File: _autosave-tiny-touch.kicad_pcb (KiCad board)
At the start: 2 copper layers, 100.3 x 76 mm, 122 parts, among them IC1 STM32F072VBT6, Q1 DTC123J, SW1 SW_Push, U1 MCP1700-3002E_SOT23, U2 SRV05-4

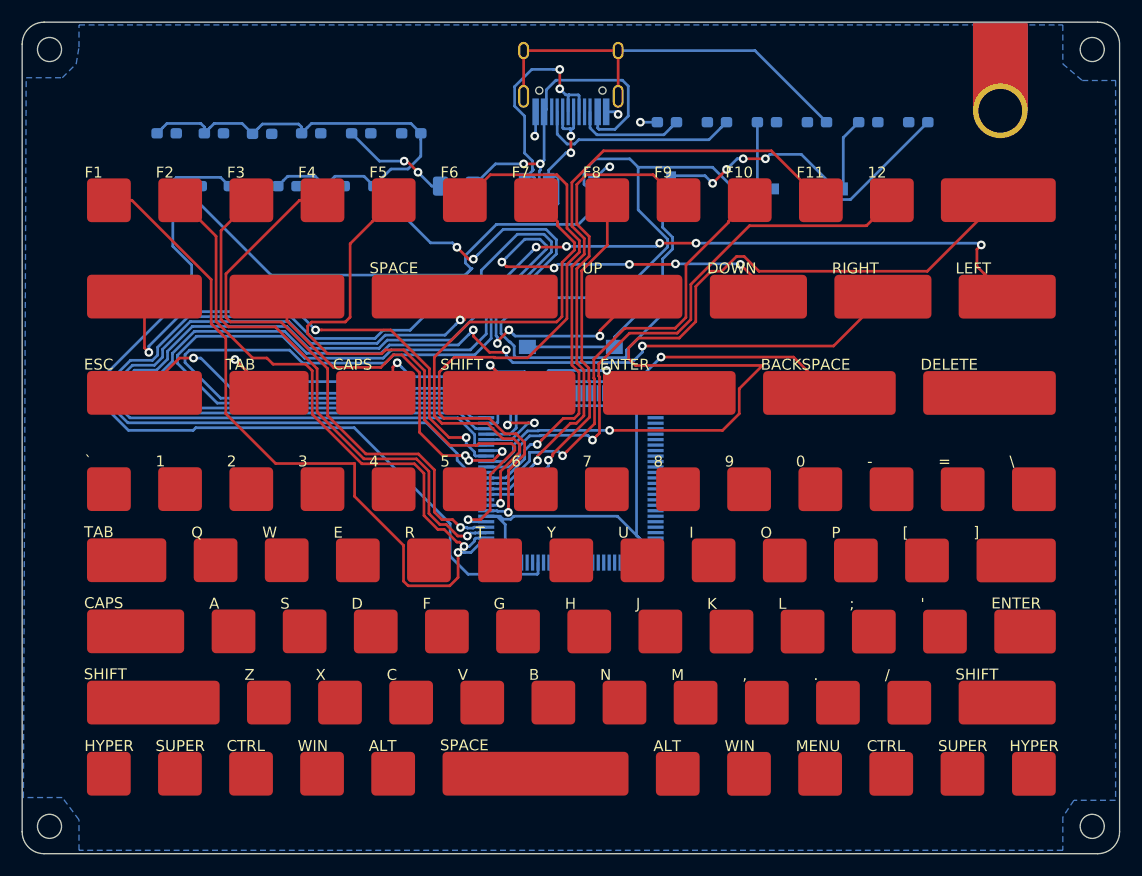
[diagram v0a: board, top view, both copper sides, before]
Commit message: Try to add more traces
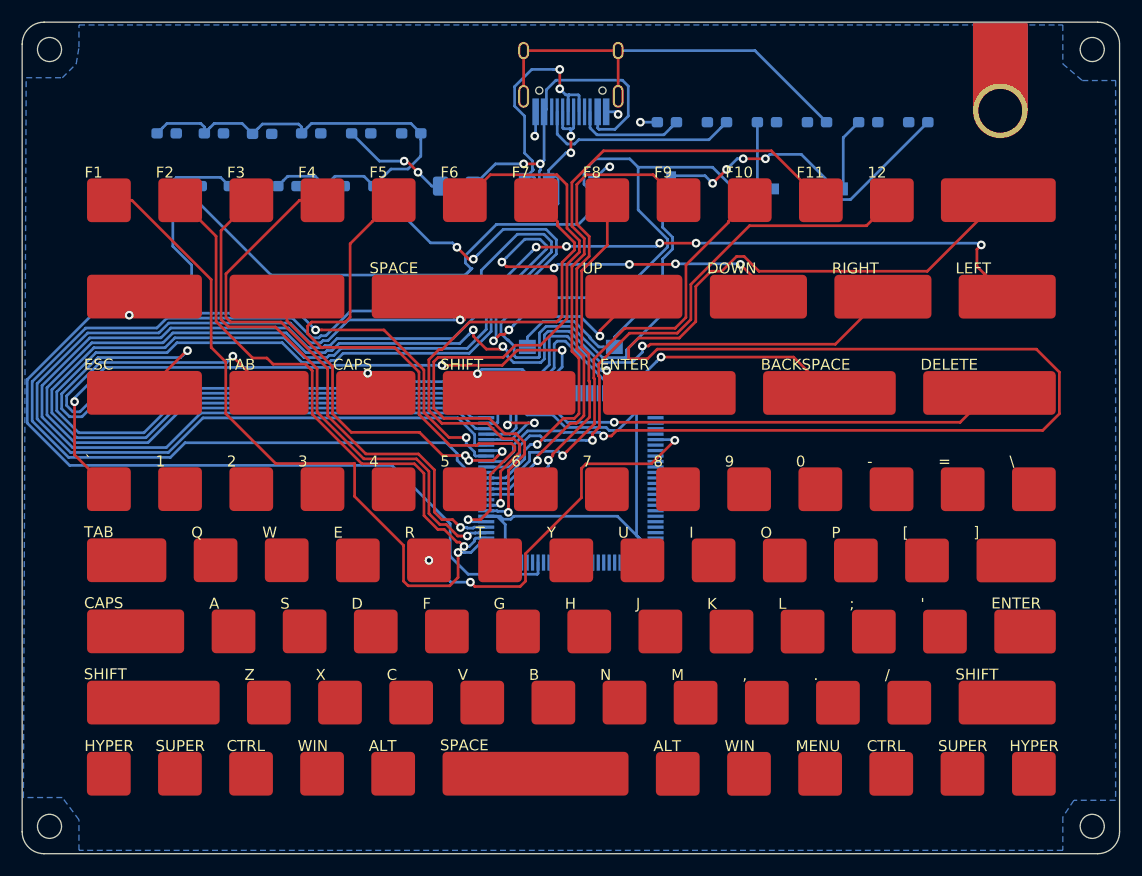
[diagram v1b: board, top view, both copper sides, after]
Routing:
- net B0: track 0.00 -> 60.2 mm, vias 0 -> 3
- net C1: track 86.5 -> 142.7 mm
- net C5: track 0.00 -> 43.0 mm, vias 0 -> 1
- net D9: track 0.00 -> 33.8 mm, vias 0 -> 3
- net A4: track 32.9 -> 66.3 mm
- net A0: track 104.6 -> 131.4 mm
- net A3: track 35.6 -> 61.7 mm
- net A2: track 118.3 -> 144.2 mm
- net A1: track 113.1 -> 134.0 mm
- net F3: track 112.0 -> 130.3 mm
- net F2: track 76.3 -> 93.5 mm
- net NRST: track 127.0 -> 142.7 mm
- net BOOTO: track 86.1 -> 100.3 mm
- net +3V3: track 196.9 -> 202.8 mm
- net C4: track 29.4 -> 34.0 mm
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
